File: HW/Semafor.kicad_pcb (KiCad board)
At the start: 2 copper layers, 160 x 160 mm, 24 parts, among them SW1 SW_Push, SW2 SW_Push, SW3 SW_Push, SW4 SW_Push, SW5 SW_Push, U1 ESP32-C3

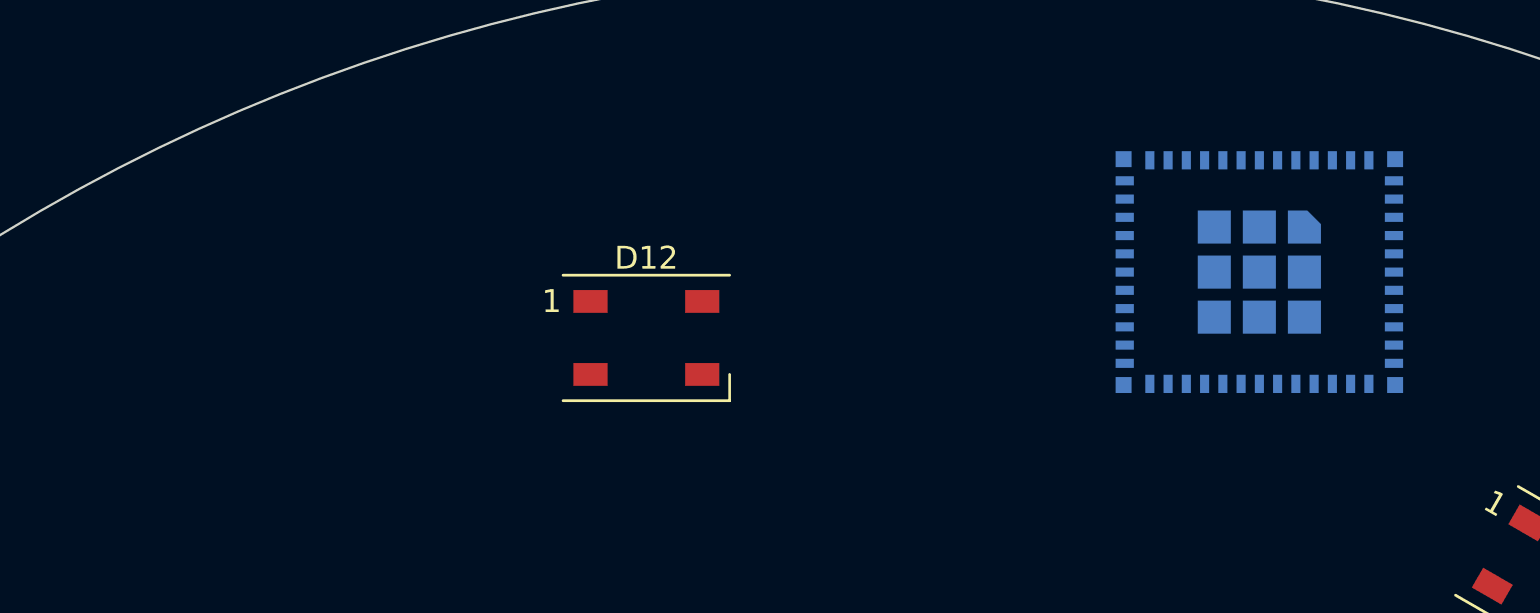
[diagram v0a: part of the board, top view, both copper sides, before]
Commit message: schematic with MCU, USB-C, LEDs, buttons, level shifter and step up
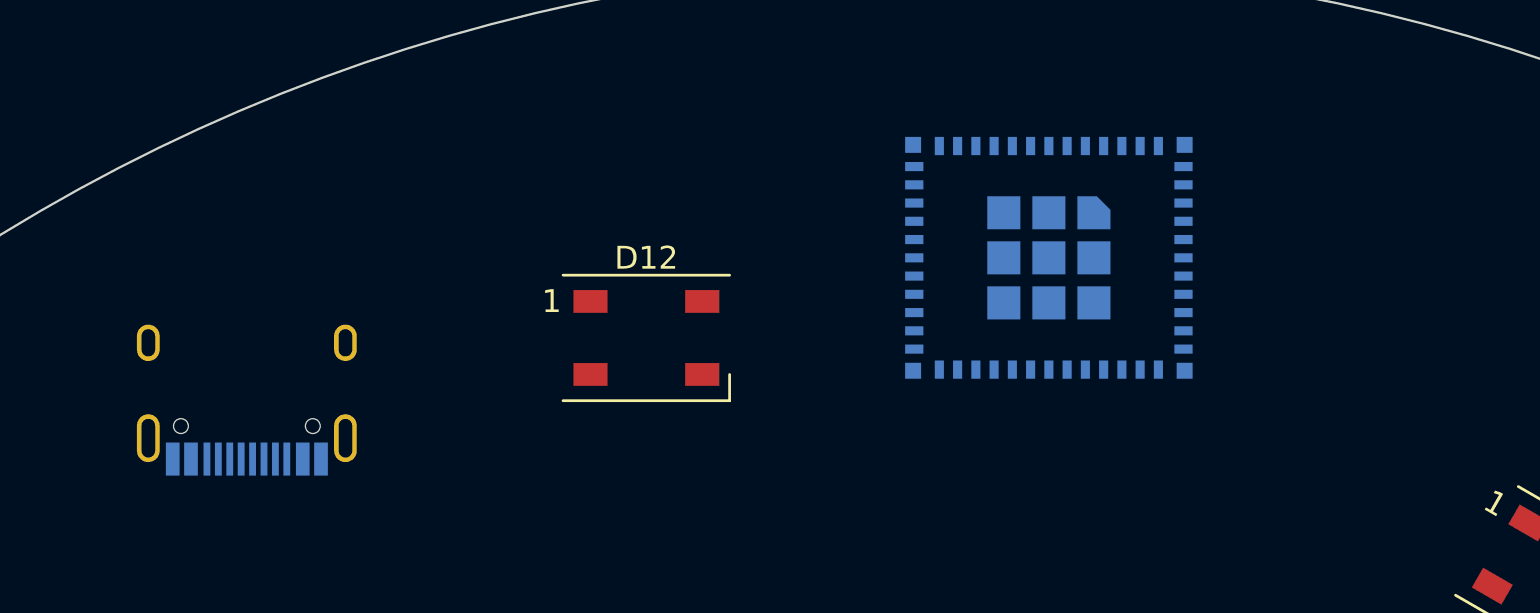
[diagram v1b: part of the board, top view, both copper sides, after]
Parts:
- added J1: USB_C_Receptacle_USB2.0, Connector_USB:USB_C_Receptacle_HRO_TYPE-C-31-M-12, B.Cu at (-159.4, 44.7)
- moved U1 9.25 mm to (-124.2, 39.9)
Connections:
- BT1 pad 1: unconnected-(BT1-Pad1) -> +3V3
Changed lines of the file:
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@@
   (net 50 "unconnected-(D12-Pad2)")
   (net 51 "+3V3")
-  (net 52 "unconnected-(BT1-Pad1)")
+  (net 52 "Net-(J1-PadA4)")
+  (net 53 "unconnected-(J1-PadA5)")
+  (net 54 "D+")
+  (net 55 "D-")
+  (net 56 "unconnected-(J1-PadA8)")
+  (net 57 "unconnected-(J1-PadB5)")
+  (net 58 "unconnected-(J1-PadB8)")
+  (net 59 "unconnected-(J1-PadS1)")
   (footprint "Button_Switch_SMD:SW_SPST_TL3342" (layer "F.Cu")
     (at -127.7 105.05)
@@
     (fp_line (start 39 -10) (end 39 10) (layer "F.SilkS") (width 0.6))
     (pad "1" thru_hole oval (at 37.35 0.05) (size 1.524 2.9) (drill oval 0.762 1.6) (layers *.Cu *.Mask)
-      (net 52 "unconnected-(BT1-Pad1)") (pinfunction "+") (pintype "passive"))
+      (net 51 "+3V3") (pinfunction "+") (pintype "passive"))
     (pad "2" thru_hole oval (at -36.35 0.05) (size 1.524 2.9) (drill oval 0.762 1.6) (layers *.Cu *.Mask)
       (net 1 "GND") (pinfunction "-") (pintype "passive"))
@@
     )
   )
-  (footprint "Library:ESP32-C3" (layer "B.Cu")
-    (at -115 40.525 180)
+  (footprint "Connector_USB:USB_C_Receptacle_HRO_TYPE-C-31-M-12" (layer "B.Cu")
+    (at -159.375 44.675)
+    (descr "USB Type-C receptacle for USB 2.0 and PD, http://www.krhro.com/uploads/soft/180320/1-1P320120243.pdf")
+    (tags "usb usb-c 2.0 pd")
     (property "Sheetfile" "Semafor.kicad_sch")
     (property "Sheetname" "")
+    (attr smd)
+    (fp_text reference "J1" (at 0 5.645) (layer "B.SilkS")
+      (effects (font (size 1 1) (thickness 0.15)) (justify mirror))
+    )
+    (fp_text value "USB_C_Receptacle_USB2.0" (at 0 -5.1) (layer "B.Fab")
+      (effects (font (size 1 1) (thickness 0.15)) (justify mirror))
+    )
+    (fp_text user "${REFERENCE}" (at 0 0) (layer "B.Fab")
+      (effects (font (size 1 1) (thickness 0.15)) (justify mirror))
+    )
+    (fp_line (start -4.7 -3.9) (end 4.7 -3.9) (layer "B.SilkS") (width 0.12))
+    (fp_line (start 4.7 1.9) (end 4.7 -0.1) (layer "B.SilkS") (width 0.12))
+    (fp_line (start -4.7 -2) (end -4.7 -3.9) (layer "B.SilkS") (width 0.12))
+    (fp_line (start -4.7 1.9) (end -4.7 -0.1) (layer "B.SilkS") (width 0.12))
+    (fp_line (start 4.7 -2) (end 4.7 -3.9) (layer "B.SilkS") (width 0.12))
+    (fp_line (start -5.32 5.27) (end 5.32 5.27) (layer "B.CrtYd") (width 0.05))
+    (fp_line (start 5.32 5.27) (end 5.32 -4.15) (layer "B.CrtYd") (width 0.05))
+    (fp_line (start -5.32 5.27) (end -5.32 -4.15) (layer "B.CrtYd") (width 0.05))
+    (fp_line (start -5.32 -4.15) (end 5.32 -4.15) (layer "B.CrtYd") (width 0.05))
+    (fp_line (start -4.47 3.65) (end 4.47 3.65) (layer "B.Fab") (width 0.1))
+    (fp_line (start -4.47 3.65) (end -4.47 -3.65) (layer "B.Fab") (width 0.1))
+    (fp_line (start -4.47 -3.65) (end 4.47 -3.65) (layer "B.Fab") (width 0.1))
+    (fp_line (start 4.47 3.65) (end 4.47 -3.65) (layer "B.Fab") (width 0.1))
+    (pad "" np_thru_hole circle (at -2.89 2.6) (size 0.65 0.65) (drill 0.65) (layers *.Cu *.Mask))
+    (pad "" np_thru_hole circle (at 2.89 2.6) (size 0.65 0.65) (drill 0.65) (layers *.Cu *.Mask))
+    (pad "A1" smd rect (at -3.25 4.045) (size 0.6 1.45) (layers "B.Cu" "B.Paste" "B.Mask")
+      (net 1 "GND") (pinfunction "GND") (pintype "passive"))
+    (pad "A4" smd rect (at -2.45 4.045) (size 0.6 1.45) (layers "B.Cu" "B.Paste" "B.Mask")
+      (net 52 "Net-(J1-PadA4)") (pinfunction "VBUS") (pintype "passive"))
+    (pad "A5" smd rect (at -1.25 4.045) (size 0.3 1.45) (layers "B.Cu" "B.Paste" "B.Mask")
+      (net 53 "unconnected-(J1-PadA5)") (pinfunction "CC1") (pintype "bidirectional"))
+    (pad "A6" smd rect (at -0.25 4.045) (size 0.3 1.45) (layers "B.Cu" "B.Paste" "B.Mask")
+      (net 54 "D+") (pinfunction "D+") (pintype "bidirectional"))
+    (pad "A7" smd rect (at 0.25 4.045) (size 0.3 1.45) (layers "B.Cu" "B.Paste" "B.Mask")
+      (net 55 "D-") (pinfunction "D-") (pintype "bidirectional"))
+    (pad "A8" smd rect (at 1.25 4.045) (size 0.3 1.45) (layers "B.Cu" "B.Paste" "B.Mask")
+      (net 56 "unconnected-(J1-PadA8)") (pinfunction "SBU1") (pintype "bidirectional"))
+    (pad "A9" smd rect (at 2.45 4.045) (size 0.6 1.45) (layers "B.Cu" "B.Paste" "B.Mask")
+      (net 52 "Net-(J1-PadA4)") (pinfunction "VBUS") (pintype "passive"))
+    (pad "A12" smd rect (at 3.25 4.045) (size 0.6 1.45) (layers "B.Cu" "B.Paste" "B.Mask")
+      (net 1 "GND") (pinfunction "GND") (pintype "passive"))
+    (pad "B1" smd rect (at 3.25 4.045) (size 0.6 1.45) (layers "B.Cu" "B.Paste" "B.Mask")
+      (net 1 "GND") (pinfunction "GND") (pintype "passive"))
+    (pad "B4" smd rect (at 2.45 4.045) (size 0.6 1.45) (layers "B.Cu" "B.Paste" "B.Mask")
+      (net 52 "Net-(J1-PadA4)") (pinfunction "VBUS") (pintype "passive"))
+    (pad "B5" smd rect (at 1.75 4.045) (size 0.3 1.45) (layers "B.Cu" "B.Paste" "B.Mask")
+      (net 57 "unconnected-(J1-PadB5)") (pinfunction "CC2") (pintype "bidirectional"))
+    (pad "B6" smd rect (at 0.75 4.045) (size 0.3 1.45) (layers "B.Cu" "B.Paste" "B.Mask")
+      (net 54 "D+") (pinfunction "D+") (pintype "bidirectional"))
+    (pad "B7" smd rect (at -0.75 4.045) (size 0.3 1.45) (layers "B.Cu" "B.Paste" "B.Mask")
+      (net 55 "D-") (pinfunction "D-") (pintype "bidirectional"))
+    (pad "B8" smd rect (at -1.75 4.045) (size 0.3 1.45) (layers "B.Cu" "B.Paste" "B.Mask")
+      (net 58 "unconnected-(J1-PadB8)") (pinfunction "SBU2") (pintype "bidirectional"))
+    (pad "B9" smd rect (at -2.45 4.045) (size 0.6 1.45) (layers "B.Cu" "B.Paste" "B.Mask")
+      (net 52 "Net-(J1-PadA4)") (pinfunction "VBUS") (pintype "passive"))
+    (pad "B12" smd rect (at -3.25 4.045) (size 0.6 1.45) (layers "B.Cu" "B.Paste" "B.Mask")
+      (net 1 "GND") (pinfunction "GND") (pintype "passive"))
+    (pad "S1" thru_hole oval (at 4.32 -1.05) (size 1 1.6) (drill oval 0.6 1.2) (layers *.Cu *.Mask)
+      (net 59 "unconnected-(J1-PadS1)") (pinfunction "SHIELD") (pintype "passive+no_connect"))
+    (pad "S1" thru_hole oval (at -4.32 3.13) (size 1 2.1) (drill oval 0.6 1.7) (layers *.Cu *.Mask)
+      (net 59 "unconnected-(J1-PadS1)") (pinfunction "SHIELD") (pintype "passive+no_connect"))
+    (pad "S1" thru_hole oval (at -4.32 -1.05) (size 1 1.6) (drill oval 0.6 1.2) (layers *.Cu *.Mask)
+      (net 59 "unconnected-(J1-PadS1)") (pinfunction "SHIELD") (pintype "passive+no_connect"))
+    (pad "S1" thru_hole oval (at 4.32 3.13) (size 1 2.1) (drill oval 0.6 1.7) (layers *.Cu *.Mask)
+      (net 59 "unconnected-(J1-PadS1)") (pinfunction "SHIELD") (pintype "passive+no_connect"))
+    (model "${KICAD6_3DMODEL_DIR}/Connector_USB.3dshapes/USB_C_Receptacle_HRO_TYPE-C-31-M-12.wrl"
+      (offset (xyz 0 0 0))
+      (scale (xyz 1 1 1))
+      (rotate (xyz 0 0 0))
+    )
+  )
+  (footprint "Library:ESP32-C3" (layer "B.Cu")
+    (at -124.225 39.9 180)
+    (property "Sheetfile" "Semafor.kicad_sch")
+    (property "Sheetname" "")

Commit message: basic placing units
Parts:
- added C1: 4u7, Capacitor_SMD:C_0805_2012Metric, B.Cu at (49.8, 162.8)
- added C10: 4u7, Capacitor_SMD:C_0805_2012Metric, B.Cu at (37.3, 163.8)
- added C11: 1u, Capacitor_SMD:C_0805_2012Metric, B.Cu at (80.3, 97.5)
- added C12: 1u, Capacitor_SMD:C_0805_2012Metric, B.Cu at (84.2, 97.8)
- added C13: 4u7, Capacitor_SMD:C_0805_2012Metric, B.Cu at (93.2, 152.1)
- added C14: 10u, Capacitor_SMD:C_0805_2012Metric, B.Cu at (103.2, 151.9)
- added C2: 1u, Capacitor_SMD:C_0805_2012Metric, B.Cu at (103.8, 100.5)
- added C8: 10u, Capacitor_SMD:C_0805_2012Metric, B.Cu at (103.3, 89.7)
- added C9: 100n, Capacitor_SMD:C_0805_2012Metric, B.Cu at (108.0, 89.8)
- added D13: Green, LED_SMD:LED_0603_1608Metric, B.Cu at (34.0, 160.2)
- added D14: Red, LED_SMD:LED_0603_1608Metric, B.Cu at (37.4, 159.2)
- added D15: Green, LED_SMD:LED_0603_1608Metric, B.Cu at (132.6, 113.0)
- added D16: Green, LED_SMD:LED_0603_1608Metric, B.Cu at (132.5, 117.4)
- added D17: MBR0520, Diode_SMD:D_SOD-123, B.Cu at (104.2, 146.5)
- added L1: 5u6, Inductor_SMD:L_6.3x6.3_H3, B.Cu at (97.2, 145.3)
- added Q1: Q_NMOS_GSD, Package_TO_SOT_SMD:SOT-23, B.Cu at (148.8, 81.0)
- added R1: 10k, Resistor_SMD:R_0603_1608Metric, B.Cu at (152.6, 80.9)
- added R10: 13k3, Resistor_SMD:R_0603_1608Metric, B.Cu at (97.8, 155.4)
- added R11: 10k, Resistor_SMD:R_0603_1608Metric, B.Cu at (136.0, 113.0)
- added R12: 10k, Resistor_SMD:R_0603_1608Metric, B.Cu at (135.9, 117.3)
- added R2: 5k1, Resistor_SMD:R_0603_1608Metric, B.Cu at (46.8, 71.2)
- added R3: 5k1, Resistor_SMD:R_0603_1608Metric, B.Cu at (51.2, 71.2)
- added R4: 10k, Resistor_SMD:R_0603_1608Metric, B.Cu at (145.2, 79.9)
- added R5: 10k, Resistor_SMD:R_0603_1608Metric, B.Cu at (103.6, 96.7)
- added R6: 330R, Resistor_SMD:R_0603_1608Metric, B.Cu at (37.2, 155.6)
- added R7: 10k, Resistor_SMD:R_0603_1608Metric, B.Cu at (103.0, 93.0)
- added R8: 1k2, Resistor_SMD:R_0603_1608Metric, B.Cu at (49.8, 159.8)
- added R9: 40k2, Resistor_SMD:R_0603_1608Metric, B.Cu at (101.6, 155.5)
- added SW6: SW_SPDT, Connector_PinSocket_2.54mm:PinSocket_1x03_P2.54mm_Vertical, F.Cu at (53.9, 111.7)
- added U2: CN3058E, Package_SO:SOP-8_3.76x4.96mm_P1.27mm, B.Cu at (43.3, 160.6)
- added U3: LT1930, Package_TO_SOT_SMD:SOT-23-5, B.Cu at (97.2, 152.0)
- BT1: moved to B.Cu
- moved BT1 291.8 mm to (157.4, 44.5), turned to 180 degrees
- moved U1 224.7 mm to (94.2, 93.0)
- moved J1 209.6 mm to (49.5, 63.2)
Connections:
- BT1 pad 1: +3V3 -> Net-(BT1-Pad1)
- D1 pad 1: +5V -> 5V_LED
- D1 pad 4: /LEDs/DATA_LED -> DATA_LED
- D10 pad 1: +5V -> 5V_LED
- D11 pad 1: +5V -> 5V_LED
- D12 pad 1: +5V -> 5V_LED
- D2 pad 1: +5V -> 5V_LED
- D3 pad 1: +5V -> 5V_LED
- D4 pad 1: +5V -> 5V_LED
- D5 pad 1: +5V -> 5V_LED
- D6 pad 1: +5V -> 5V_LED
- D7 pad 1: +5V -> 5V_LED
- D8 pad 1: +5V -> 5V_LED
- D9 pad 1: +5V -> 5V_LED
- J1 pad A4: Net-(J1-PadA4) -> +5V
- J1 pad A5: unconnected-(J1-PadA5) -> Net-(J1-PadA5)
- J1 pad A9: Net-(J1-PadA4) -> +5V
- J1 pad B4: Net-(J1-PadA4) -> +5V
- J1 pad B5: unconnected-(J1-PadB5) -> Net-(J1-PadB5)
- J1 pad B9: Net-(J1-PadA4) -> +5V
- U1 pad 16: unconnected-(U1-Pad16) -> DATA_LED_ESP
- U1 pad 26: unconnected-(U1-Pad26) -> D-
- U1 pad 27: unconnected-(U1-Pad27) -> D+
- U1 pad 48: (no net) -> GND
- U1 pad 5: unconnected-(U1-Pad5) -> Net-(U1-Pad5)
- U1 pad 8: unconnected-(U1-Pad8) -> Net-(U1-Pad8)

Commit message: change value of inductor, update PCB, repair connection step up of pin /SHDN, delete capacitors from ESP32
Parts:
- removed C11, C12: 1u, Capacitor_SMD:C_0805_2012Metric
- added R13: 150k, Resistor_SMD:R_0603_1608Metric, B.Cu at (102.2, 125.5)
- L1: value 5u6 -> 4u7; footprint Inductor_SMD:L_6.3x6.3_H3 -> Library:L_CDRH3D18
- R10: value 13k3 -> 22k
- R9: value 40k2 -> 10k
- moved C1 116.1 mm to (115.2, 66.8)
- moved C10 116.1 mm to (102.7, 67.8)
- moved D13 116.1 mm to (99.4, 64.2)
- moved D14 116.1 mm to (102.7, 63.2)
- moved R6 116.1 mm to (102.6, 59.6)
- moved R8 116.1 mm to (115.1, 63.8)
- moved U2 116.1 mm to (108.7, 64.6)
- moved D15 67.8 mm to (117.4, 46.9)
- moved R11 67.8 mm to (120.8, 46.9)
- moved R2 58.8 mm to (100.4, 47.0)
- moved R3 57.5 mm to (103.4, 47.0)
- moved Q1 57.1 mm to (149.4, 138.1)
- moved R1 57.1 mm to (153.1, 138.0)
- moved R4 57.1 mm to (145.8, 137.0)
- moved J1 57.0 mm to (101.6, 40.2)
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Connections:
- C14 pad 1: 5V_LED -> PWR_LED
- D1 pad 1: 5V_LED -> PWR_LED
- D10 pad 1: 5V_LED -> PWR_LED
- D11 pad 1: 5V_LED -> PWR_LED
- D12 pad 1: 5V_LED -> PWR_LED
- D17 pad 1: 5V_LED -> PWR_LED
- D2 pad 1: 5V_LED -> PWR_LED
- D3 pad 1: 5V_LED -> PWR_LED
- D4 pad 1: 5V_LED -> PWR_LED
- D5 pad 1: 5V_LED -> PWR_LED
- D6 pad 1: 5V_LED -> PWR_LED
- D7 pad 1: 5V_LED -> PWR_LED
- D8 pad 1: 5V_LED -> PWR_LED
- D9 pad 1: 5V_LED -> PWR_LED
- R4 pad 1: +5V -> PWR_LED
- R9 pad 1: 5V_LED -> PWR_LED
- U3 pad 4: unconnected-(U3-Pad4) -> Net-(U3-Pad4)
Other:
- board size 160 x 160 mm -> 200 x 200 mm
- board text added: "step up"
